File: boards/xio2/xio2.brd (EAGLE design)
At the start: 170 x 100 mm, 348 parts, among them J1 12401598E4#2A, Q1 BSS138, Q2 BSS138, Q3 BC817-16LT3G, Q4 BC817-16LT3G, Y2 FA-238 25.0000MB-K3

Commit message: Minor changes
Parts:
- moved HOST_IO 1.80 mm to (83.3, 1.23)

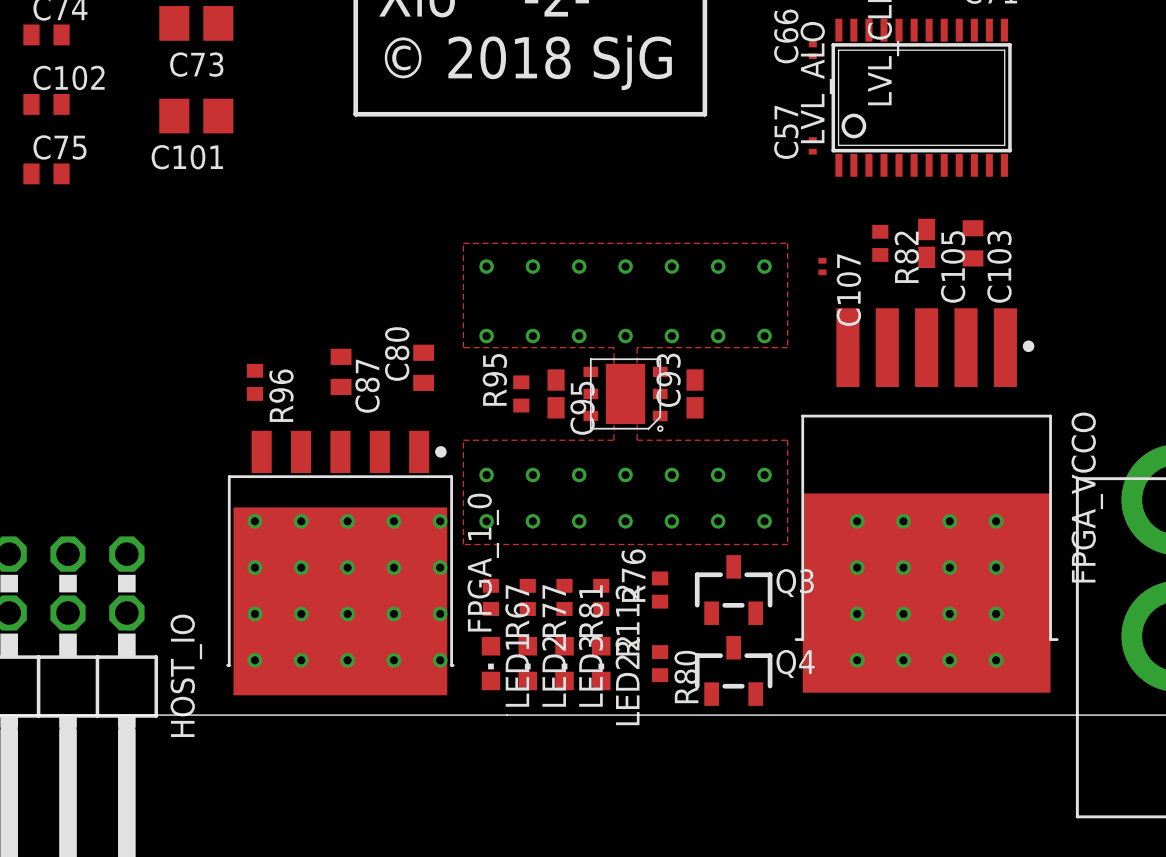
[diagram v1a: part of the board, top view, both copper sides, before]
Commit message: Incorporate the changes from the design-review, including switching regulator for 1.0v
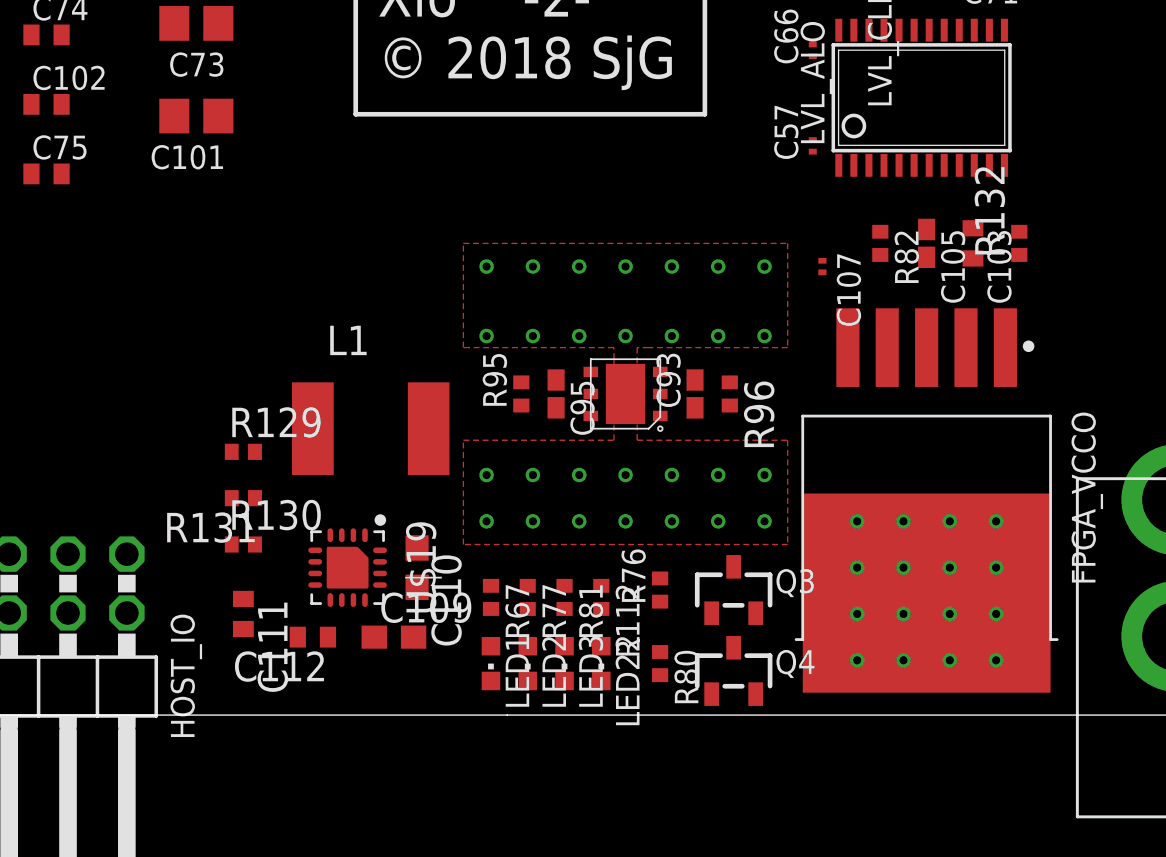
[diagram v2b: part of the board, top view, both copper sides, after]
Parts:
- removed C80, C87: 4.7uF, rcl:C0402
- removed FPGA_1_0: MIC49200-1.0WRSPAK-5, sjg-power:TO170P1055X205-6
- added C109, C110: 22uF, rcl:C0603
- added C111: 0.01uF, rcl:C0402
- added C112: 3900pF, rcl:C0402
- added L1: 1.5uH, rcl:L5650M
- added R129: 499K, rcl:R0402
- added R130: 40.2K, rcl:R0402
- added R131: 160K, rcl:R0402
- added R132: 10K, rcl:R0402
- added U$19: TLV62095, sjg-power:QFN50P310X310X100-16
- R96: value 0R -> 10K
- moved R96 20.5 mm to (133.5, 14.5)
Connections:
- removed net N$83: C87.1, FPGA_1_0.5, R96.2
- new net N$64: C111.1, U$19.7
- new net N$72: C111.2, U$19.8
- new net N$73: L1.1, U$19.1, U$19.2
- new net N$79: R130.2, R131.1, U$19.5
- new net N$98: C112.1, U$19.9
- new net PGOOD_10: FPGA_1_8.P3, R129.2, R96.1, U$19.4
- net +5V: now also C109.1, R129.1, U$19.10, U$19.11, U$19.12, U$19.13, U$19.3; no longer C80.1, FPGA_1_0.1, FPGA_1_0.2, FPGA_1_0.4
- net GND: now also C109.2, C110.2, C112.2, R131.2, R132.2, R96.2, U$19.14, U$19.15, U$19.6, U$19.PAD; no longer C80.2, C87.2, FPGA_1_0.3, FPGA_1_0.6
- net VCCAUX: now also R132.1
- net VCCINT: now also C110.1, L1.2, R130.1, U$19.16; no longer FPGA_1_8.P3, R96.1

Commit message: routed and vias
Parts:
- moved C173 5.96 mm to (19.3, 31.3), turned to 90 degrees
- moved PSW 5.10 mm to (21.4, 32.3)
- moved R119 4.00 mm to (22.3, 34.5), turned to 0 degrees
- moved C99 0.22 mm to (22.5, 55.1)
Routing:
- net GND: track 0.00 -> 910.5 mm, vias 44 -> 347
- net VCCO: track 0.00 -> 333.7 mm, vias 0 -> 35
- net HOST_A2: track 0.00 -> 327.2 mm, vias 0 -> 4
- net HOST_A11: track 0.00 -> 324.3 mm, vias 0 -> 10
- net HOST_A5: track 0.00 -> 322.4 mm, vias 0 -> 6
- net HOST_A6: track 0.00 -> 317.1 mm, vias 0 -> 9
- net HOST_A7: track 0.00 -> 301.5 mm, vias 0 -> 7
- net HOST_A12: track 0.00 -> 300.9 mm, vias 0 -> 10
- net HOST_A9: track 0.00 -> 292.2 mm, vias 0 -> 9
- net HOST_A3: track 0.00 -> 292.2 mm, vias 0 -> 9
- net HOST_A4: track 0.00 -> 292.2 mm, vias 0 -> 10
- net HOST_A0: track 0.00 -> 291.6 mm, vias 0 -> 8
- net HOST_A10: track 0.00 -> 287.2 mm, vias 0 -> 10
- net HOST_A1: track 0.00 -> 270.3 mm, vias 0 -> 11
- net HOST_A14: track 0.00 -> 264.4 mm, vias 0 -> 7
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
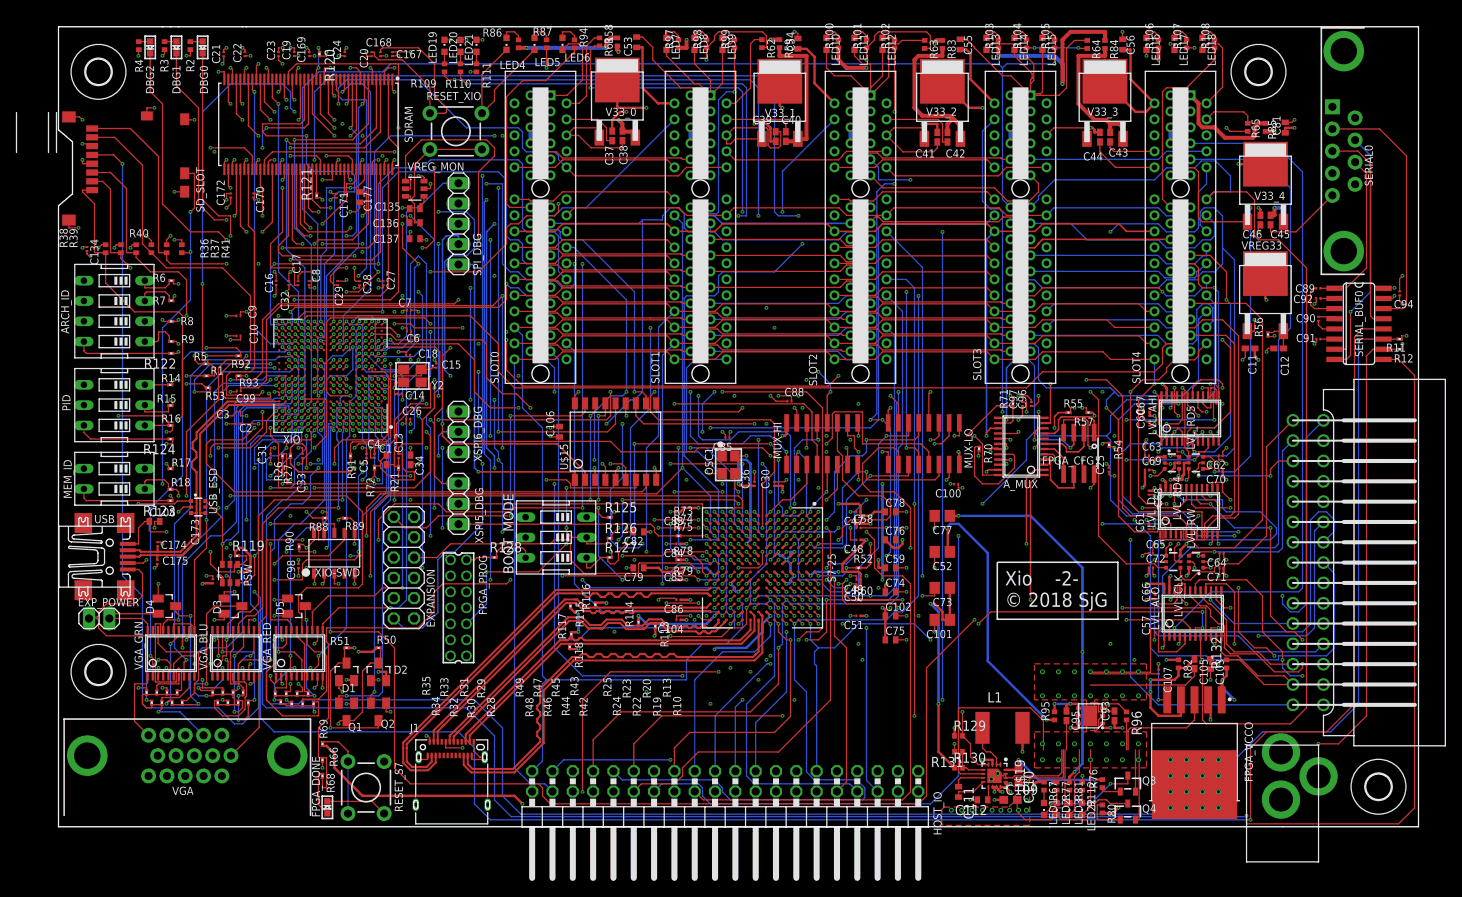
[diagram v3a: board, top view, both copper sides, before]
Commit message: Make the 5V switch have a defined area for the XIO_USB_VBUS signal, so there’s a nice path between 5v and the port, via the switch.
Also add thermal vias to the slot regulators

Also add thermal/signal vias to the PSU entry
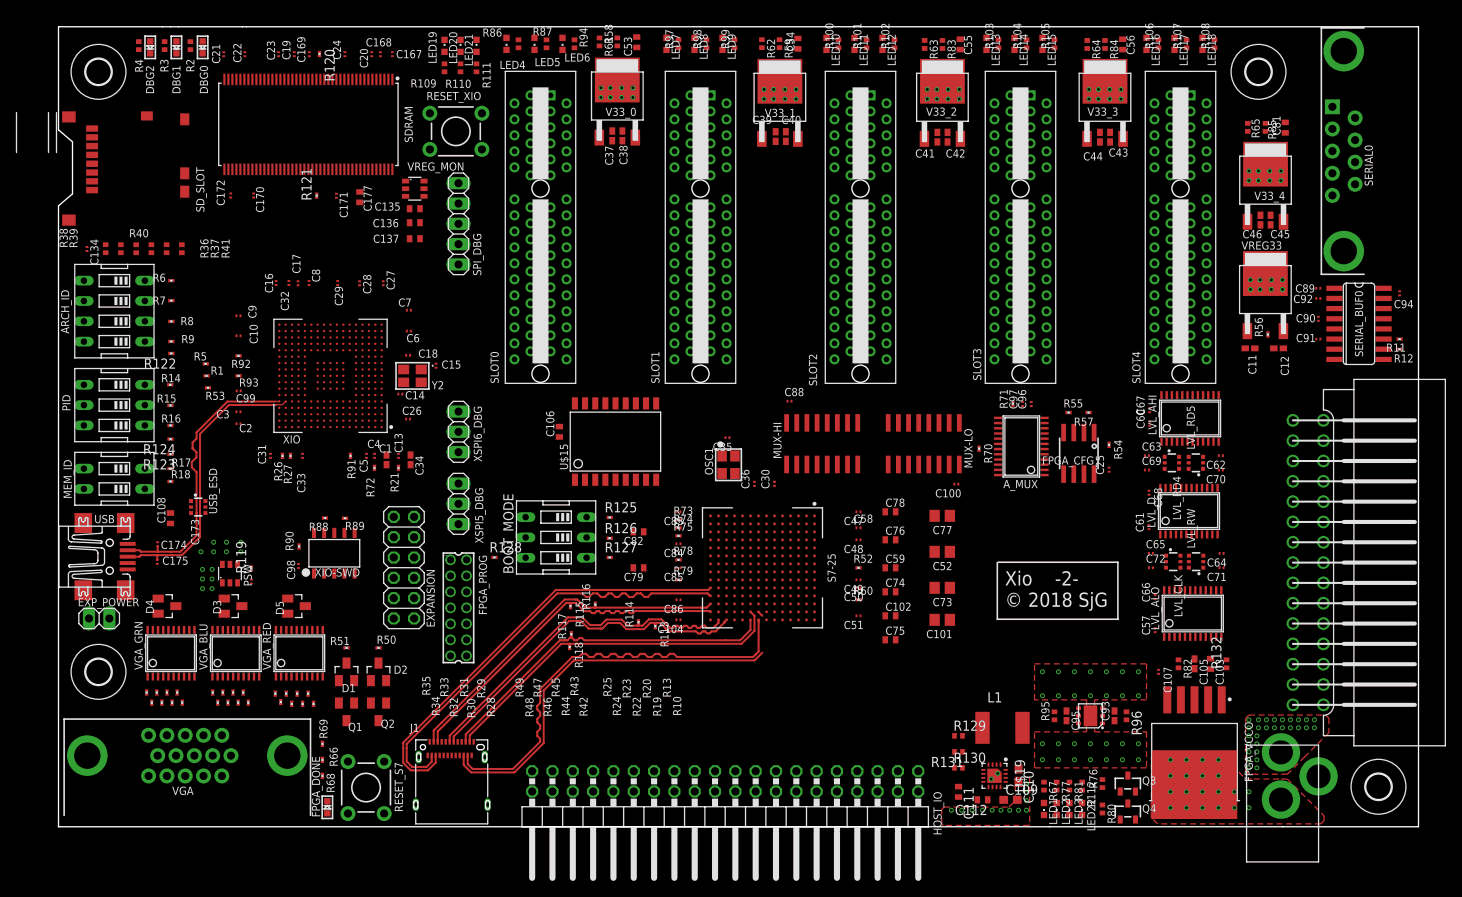
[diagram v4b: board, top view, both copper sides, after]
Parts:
- moved R123 5.80 mm to (14.0, 47.2)
- moved C173 4.82 mm to (24.1, 31.3), turned to 270 degrees
- moved R119 2.37 mm to (24.1, 32.9), turned to 90 degrees
- moved C108 2.04 mm to (14.0, 39.2), turned to 90 degrees
- moved R18 1.00 mm to (14.0, 43.8)
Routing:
- net GND: track 910.5 -> 0.00 mm, vias 347 -> 62
- net VCCO: track 333.7 -> 0.00 mm, vias 35 -> 0
- net HOST_A2: track 327.2 -> 0.00 mm, vias 4 -> 0
- net HOST_A11: track 324.3 -> 0.00 mm, vias 10 -> 0
- net HOST_A5: track 322.4 -> 0.00 mm, vias 6 -> 0
- net HOST_A6: track 317.1 -> 0.00 mm, vias 9 -> 0
- net HOST_A7: track 301.5 -> 0.00 mm, vias 7 -> 0
- net HOST_A12: track 300.9 -> 0.00 mm, vias 10 -> 0
- net HOST_A9: track 292.2 -> 0.00 mm, vias 9 -> 0
- net HOST_A3: track 292.2 -> 0.00 mm, vias 9 -> 0
- net HOST_A4: track 292.2 -> 0.00 mm, vias 10 -> 0
- net HOST_A0: track 291.6 -> 0.00 mm, vias 8 -> 0
- net HOST_A10: track 287.2 -> 0.00 mm, vias 10 -> 0
- net HOST_A1: track 270.3 -> 0.00 mm, vias 11 -> 0
- net HOST_A14: track 264.4 -> 0.00 mm, vias 7 -> 0
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- added copper zone on layer 1, net +5V
- added copper zone on layer 14, net XIO_USB_VBUS

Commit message: Improve the layout by enacting most of the notes-to-self at the bottom of the board
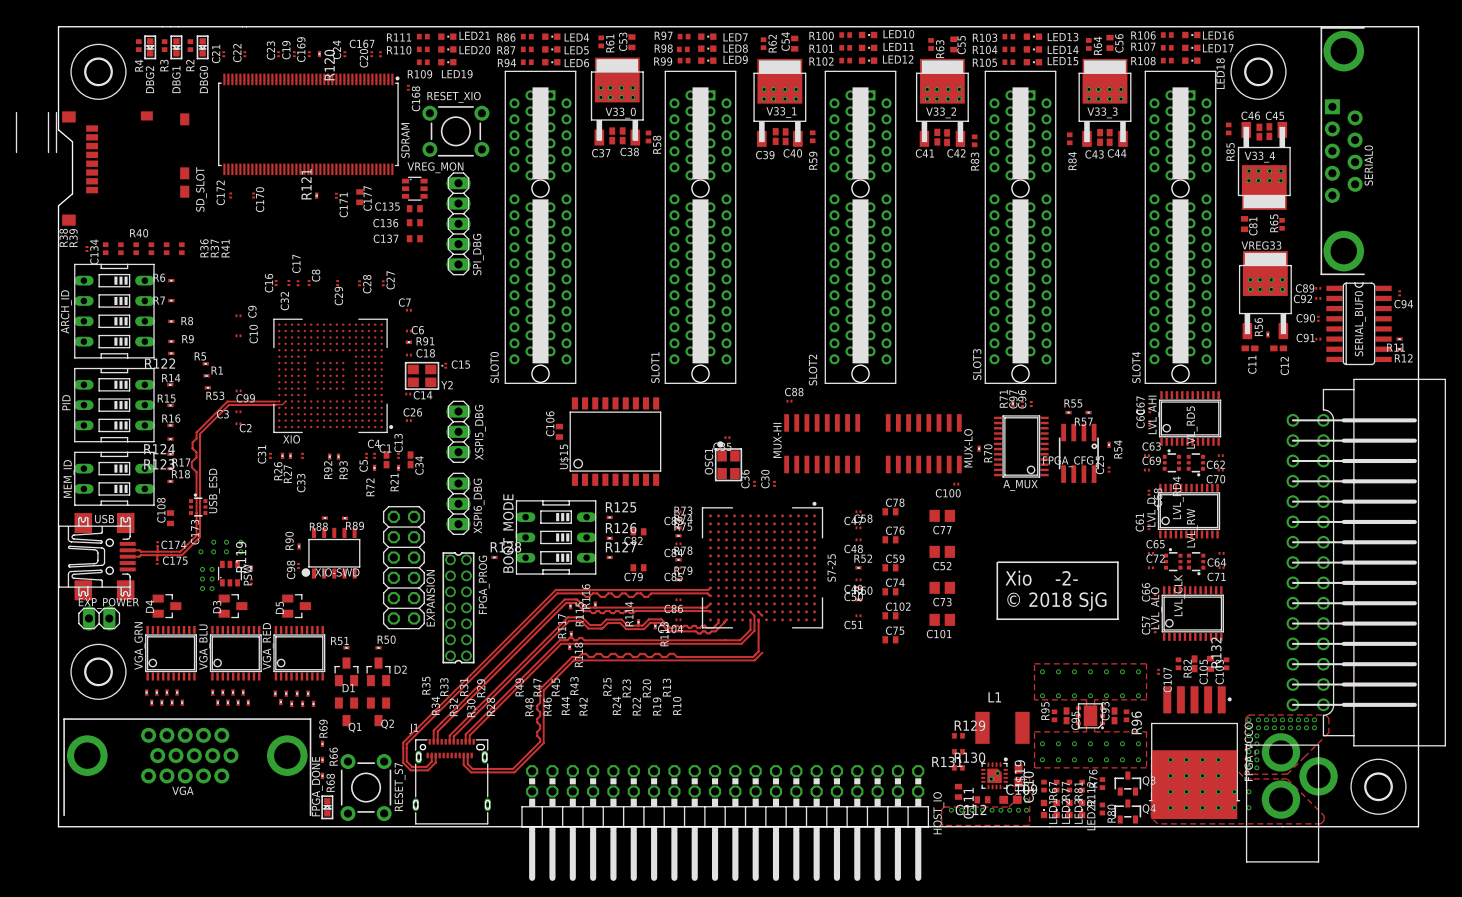
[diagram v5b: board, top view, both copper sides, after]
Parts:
- moved R92 17.0 mm to (33.9, 46.9), turned to 270 degrees
- moved R93 16.1 mm to (35.0, 46.9), turned to 270 degrees
- moved R91 16.0 mm to (43.8, 61.2), turned to 0 degrees
- moved C81 13.1 mm to (148.3, 76.0), turned to 270 degrees
- moved R65 12.9 mm to (152.9, 75.9), turned to 90 degrees
- moved R83 12.7 mm to (114.5, 86.4), turned to 90 degrees
- moved R84 12.6 mm to (126.4, 86.6)
- moved R58 12.5 mm to (73.8, 86.9), turned to 90 degrees
- moved R59 12.4 mm to (94.3, 86.9), turned to 90 degrees
- moved C45 11.1 mm to (151.4, 87.5), turned to 90 degrees
- moved C46 11.1 mm to (150.1, 87.5)
- moved XSPI5_DBG 9.00 mm to (50.0, 50.0)
- moved XSPI6_DBG 9.00 mm to (50.0, 41.0)
- moved R111 7.71 mm to (45.6, 99.4), turned to 0 degrees
- moved R99 6.64 mm to (78.2, 96.4), turned to 180 degrees
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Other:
- board text added: "Amrith recommends matched 3.3v and 5v caps to GND along 5v power plane border"
- board text removed: "Add vias on 5v->3.3v vreg pads Play with cap/resistor placement on vregs Amrith recommends matched 3.3v and 5v caps to GND along 5v power plane border Move R91 to RHS of STM Move R92, R93 to bottom of STM"

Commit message: Improve the labelling on the board. Will probably need minor tweaks once the board is finally routed
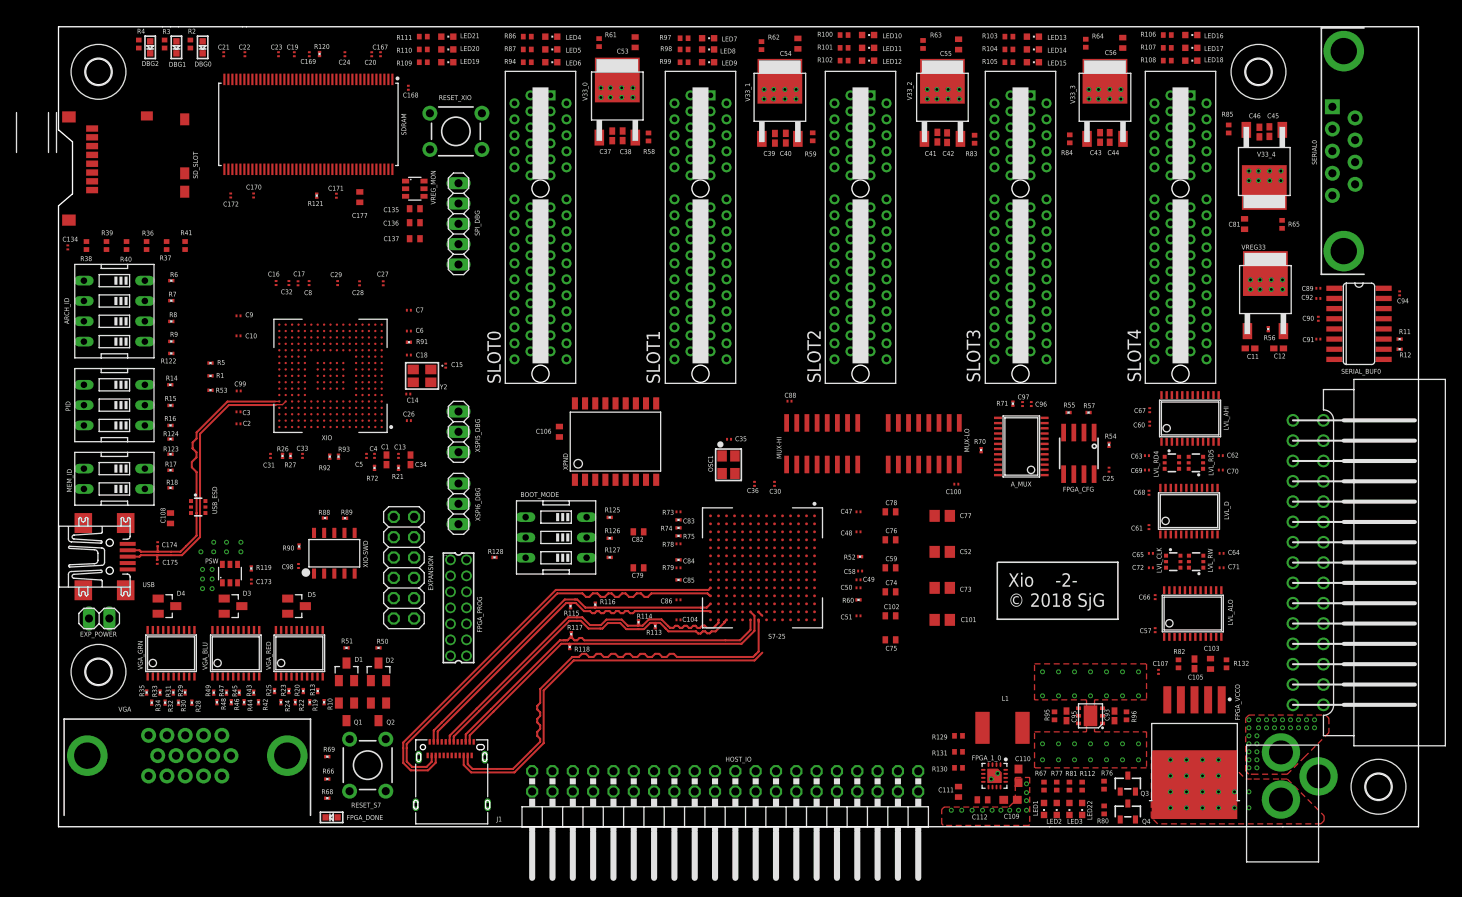
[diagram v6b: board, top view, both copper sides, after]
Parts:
- moved C58 5.40 mm to (100.2, 32.6)
- moved R68 2.86 mm to (33.6, 4.20), turned to 180 degrees
- moved RESET_S7 2.81 mm to (38.6, 8.34)
- moved R66 2.47 mm to (33.6, 6.60), turned to 0 degrees
- moved R38 2.43 mm to (3.50, 73.3)
- moved C134 2.41 mm to (1.16, 73.1)
- moved R39 1.84 mm to (6.00, 73.3)
- moved R69 1.71 mm to (33.6, 9.40), turned to 0 degrees
- moved C56 1.60 mm to (133.0, 98.6)
- moved R52 1.41 mm to (100.2, 34.4)
- moved FPGA_DONE 1.36 mm to (34.1, 1.81), turned to 90 degrees
- moved R10 1.33 mm to (33.2, 16.2)
- moved R43 1.32 mm to (24.4, 17.4)
- moved R42 1.28 mm to (25.0, 16.2)
- moved R40 1.26 mm to (8.51, 73.3)
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- renumbered U$15 to XPND, U$19 to FPGA_1_0

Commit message: Added ground-loop caps across plane boundaries as per Amrith’s recommendation
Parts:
- added C113, C114, C115, C116, C117, C118, C119, C120, C121, C122, C123, C124, C125, C126, C127, C128, C129, C130, C131, C132, C133, C138, C80, C87: 0.1uF, rcl:C0201
- moved C39 0.40 mm to (89.2, 86.7)
- moved C40 0.40 mm to (90.5, 86.7)
- moved R59 0.40 mm to (93.9, 86.9)
- moved R62 0.40 mm to (87.5, 98.3)
- moved V33_1 0.40 mm to (89.8, 93.8)
- moved C54 0.40 mm to (92.0, 98.5)
- moved C173 0.20 mm to (23.9, 31.3)
- moved R119 0.20 mm to (23.9, 32.9)
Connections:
- net +3V3: now also C123.1, C124.1, C125.1, C126.1, C127.1, C128.1, C129.1, C130.1, C131.1, C132.1, C133.1, C138.1
- net +5V: now also C113.1, C114.1, C115.1, C116.1, C117.1, C118.1, C119.1, C120.1, C121.1, C122.1, C80.1, C87.1
- net GND: now also C113.2, C114.2, C115.2, C116.2, C117.2, C118.2, C119.2, C120.2, C121.2, C122.2, C123.2, C124.2, C125.2, C126.2, C127.2, C128.2, C129.2, C130.2, C131.2, C132.2, C133.2, C138.2, C80.2, C87.2
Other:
- board text removed: "Amrith recommends matched 3.3v and 5v caps to GND along 5v power plane border"
